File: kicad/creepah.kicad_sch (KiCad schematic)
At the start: 15 parts, among them J1 Raspberry_Pi_4, M1 Motor_DC, M2 Motor_DC, M3 Motor_DC, M4 Motor_DC, U2 L298N, U3 L298N, U4 HC-SR04, U5 HC-SR04, U6 Ag9905LP

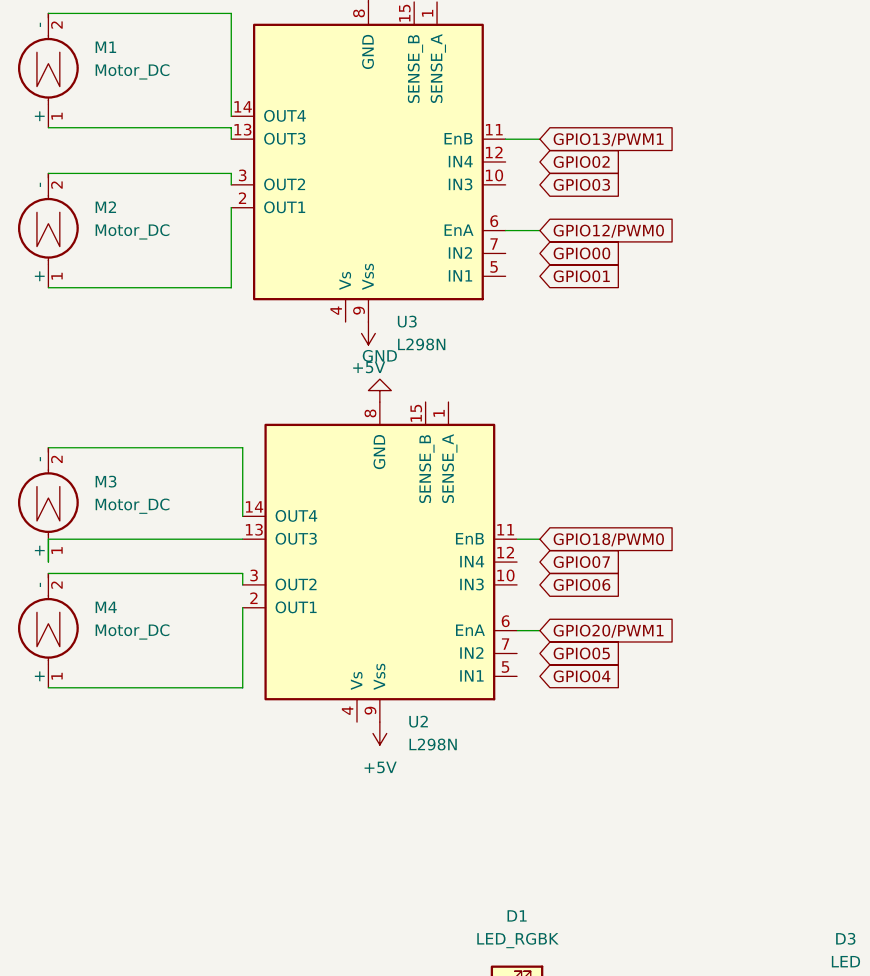
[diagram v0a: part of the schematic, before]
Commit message: Fixed motor config pins
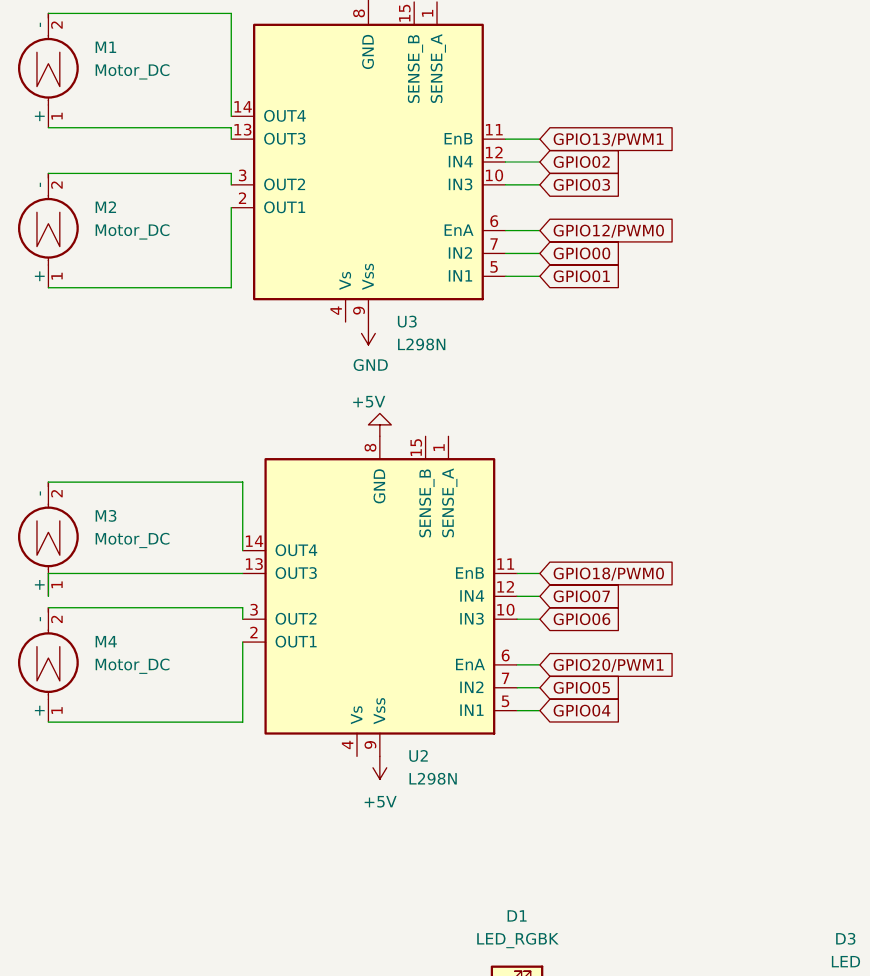
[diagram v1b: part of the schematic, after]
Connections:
- net GPIO00: now also U3.7 (IN2)
- net GPIO01: now also U3.5 (IN1)
- net GPIO02: now also U3.12 (IN4)
- net GPIO03: now also U3.10 (IN3)
- net GPIO04: now also U2.5 (IN1)
- net GPIO05: now also U2.7 (IN2)
- net GPIO06: now also U2.10 (IN3)
- net GPIO07: now also U2.12 (IN4)
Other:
- moved on the sheet: M3, M4, U2
